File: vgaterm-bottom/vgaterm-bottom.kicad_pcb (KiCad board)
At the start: 2 copper layers, 95.4 x 66.3 mm, 56 parts, among them J1 Conn_01x04 USB-UART, J10 Conn_01x14, J11 Conn_01x04, J12 Rst, J13 Conn_01x04, J2 Conn_01x04 Direct Pin, J3 DE9_Receptacle, J4 RJ45_LED, J5 DE15_Receptacle_HighDensity_M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, J6 USB_B_Micro Debug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

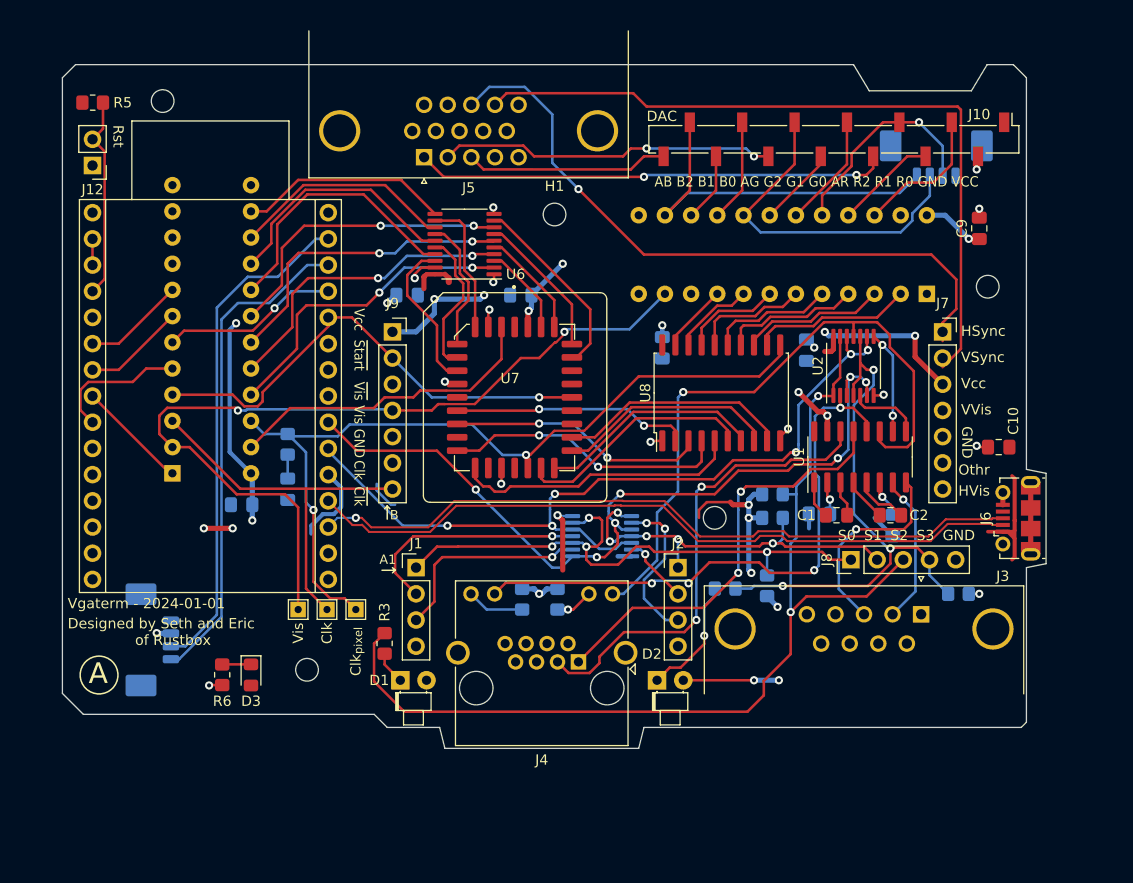
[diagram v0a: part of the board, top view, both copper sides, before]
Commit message: initial rework for all smd on one side and all IO on bottom board
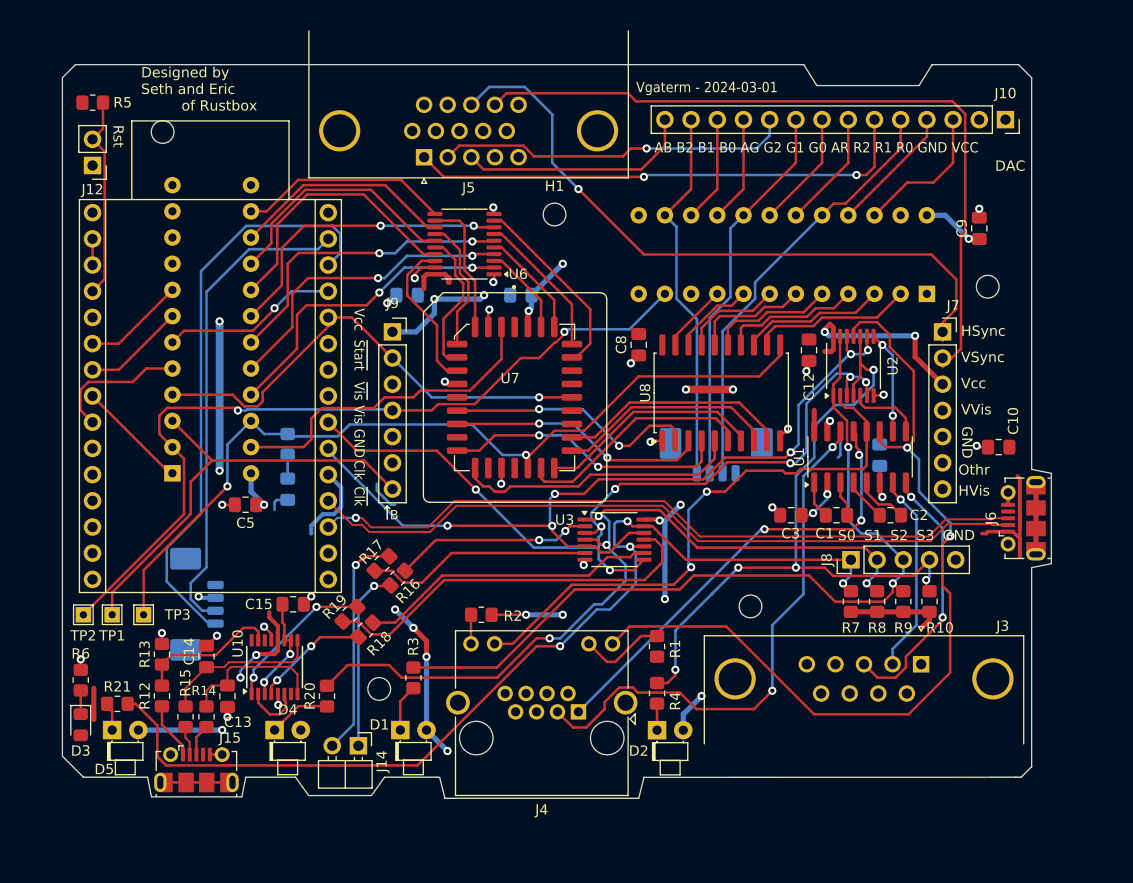
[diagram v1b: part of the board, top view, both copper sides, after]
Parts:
- removed J1: Conn_01x04 USB-UART, Connector_PinHeader_2.54mm:PinHeader_1x04_P2.54mm_Vertical
- removed J2: Conn_01x04 Direct Pin, Connector_PinHeader_2.54mm:PinHeader_1x04_P2.54mm_Vertical
- added C13: C_Small, Capacitor_SMD:C_0805_2012Metric_Pad1.18x1.45mm_HandSolder, F.Cu at (97.3, 138.7)
- added C14: C_Small, Capacitor_SMD:C_0805_2012Metric_Pad1.18x1.45mm_HandSolder, F.Cu at (95.2, 134.9)
- added C15: C_Small, Capacitor_SMD:C_0805_2012Metric_Pad1.18x1.45mm_HandSolder, F.Cu at (103.7, 129.8)
- added D4: LED, LED_THT:LED_D1.8mm_W1.8mm_H2.4mm_Horizontal_O1.27mm_Z1.6mm, F.Cu at (101.9, 142.0)
- added D5: LED, LED_THT:LED_D1.8mm_W1.8mm_H2.4mm_Horizontal_O1.27mm_Z1.6mm, F.Cu at (86.1, 142.0)
- added J14: Conn_01x02, Connector_PinHeader_2.54mm:PinHeader_1x02_P2.54mm_Horizontal, F.Cu at (110.0, 143.5)
- added J15: USB_B_Micro UART, Connector_USB:USB_Micro-B_Molex-105017-0001, F.Cu at (94.3, 145.8)
- added R12: 4.7k, Resistor_SMD:R_0805_2012Metric_Pad1.20x1.40mm_HandSolder, F.Cu at (90.9, 138.7)
- added R13: 10k, Resistor_SMD:R_0805_2012Metric_Pad1.20x1.40mm_HandSolder, F.Cu at (90.9, 134.6)
- added R14: 27, Resistor_SMD:R_0805_2012Metric_Pad1.20x1.40mm_HandSolder, F.Cu at (95.2, 140.7)
- added R15: 27, Resistor_SMD:R_0805_2012Metric_Pad1.20x1.40mm_HandSolder, F.Cu at (93.2, 140.7)
- added R16: R, Resistor_SMD:R_0805_2012Metric_Pad1.20x1.40mm_HandSolder, F.Cu at (112.3, 125.8)
- added R17: R, Resistor_SMD:R_0805_2012Metric_Pad1.20x1.40mm_HandSolder, F.Cu at (113.8, 127.3)
- added R18: R, Resistor_SMD:R_0805_2012Metric_Pad1.20x1.40mm_HandSolder, F.Cu at (109.2, 130.8)
- added R19: R, Resistor_SMD:R_0805_2012Metric_Pad1.20x1.40mm_HandSolder, F.Cu at (110.7, 132.3)
- added R20: 1k, Resistor_SMD:R_0805_2012Metric_Pad1.20x1.40mm_HandSolder, F.Cu at (106.9, 138.7)
- added R21: 1k, Resistor_SMD:R_0805_2012Metric_Pad1.20x1.40mm_HandSolder, F.Cu at (86.6, 139.4)
- added U10: FT230XS, Package_SO:SSOP-16_3.9x4.9mm_P0.635mm, F.Cu at (101.9, 135.9)
- C12, C3, C5, C8, R1, R10, R2, R4, R7, R8, R9, U3: moved to F.Cu
- J10: footprint Connector_PinSocket_2.54mm:PinSocket_1x14_P2.54mm_Vertical_SMD_Pin1Left -> Connector_PinSocket_2.54mm:PinSocket_1x14_P2.54mm_Vertical
- moved J11 35.9 mm to (144.7, 114.7)
- moved TP1 20.8 mm to (86.1, 130.8)
- moved TP2 20.8 mm to (83.3, 130.8)
- moved TP3 20.6 mm to (89.2, 130.8)
- moved D3 17.2 mm to (83.1, 141.5)
- moved J10 16.7 mm to (172.7, 82.8)
- moved R9 16.4 mm to (162.8, 129.5), turned to -90 degrees
- moved R6 13.7 mm to (83.1, 137.1), turned to 90 degrees
- moved R8 13.0 mm to (160.3, 129.5), turned to -90 degrees
- moved R4 12.1 mm to (138.9, 138.4), turned to 90 degrees
- moved R1 10.7 mm to (138.9, 133.9), turned to 90 degrees
- moved H5 9.26 mm to (148.0, 130.0)
- moved R7 8.27 mm to (157.7, 129.5)
- moved H2 7.24 mm to (112.0, 138.0)
- moved C4 6.93 mm to (160.5, 115.3), turned to -90 degrees
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- renumbered Clk to TP1, Vis to TP2, Clk_{pixel} to TP3
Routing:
- net /S_{0}: track 55.2 -> 98.1 mm
- net /S_{1}: track 38.3 -> 79.1 mm, vias 5 -> 4
- net VCC: track 122.0 -> 151.1 mm, vias 22 -> 25
- net Net-(J14-Pin_2): track 0.00 -> 22.1 mm, vias 0 -> 1
- net /R2: track 21.1 -> 42.1 mm, vias 1 -> 0
- net /TXI_{2}: track 63.7 -> 83.9 mm, vias 1 -> 2
- net Net-(J14-Pin_1): track 0.00 -> 17.7 mm, vias 0 -> 1
- net /S_{2}: track 97.8 -> 82.1 mm
- net /D-: track 0.00 -> 15.5 mm
- net /TXI_{0}: track 22.6 -> 38.0 mm, vias 1 -> 0
- net /TXI_{1}: track 6.67 -> 22.0 mm, vias 1 -> 0
- net /S_{3}: track 53.4 -> 68.8 mm, vias 3 -> 5
- net GND: track 48.8 -> 64.1 mm, vias 17 -> 26
- net Net-(U10-TXD): track 0.00 -> 15.0 mm, vias 0 -> 2
- net /D+: track 0.00 -> 14.4 mm
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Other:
- board size 95.4 x 66.3 mm -> 95.9 x 71.1 mm
- board text added: "Keyboard"
- board text added: "Vgaterm - 2024-03-01"
- board text removed: "A1"
- board text removed: "KB"
- board text removed: "Vgaterm - 2024-01-01"
